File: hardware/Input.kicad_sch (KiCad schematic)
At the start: 41 parts, among them J24 Conn_01x02, J27 USB_C_Receptacle_USB2.0, J4 AudioJack3, J5 Conn_Coaxial, J6 Conn_Coaxial, J7 Conn_Coaxial, J8 Conn_Coaxial, J9 Barrel_Jack_Switch, U23 74LVCH2T45DC, U24 74LVCH2T45DC, U25 74LVCH2T45DC

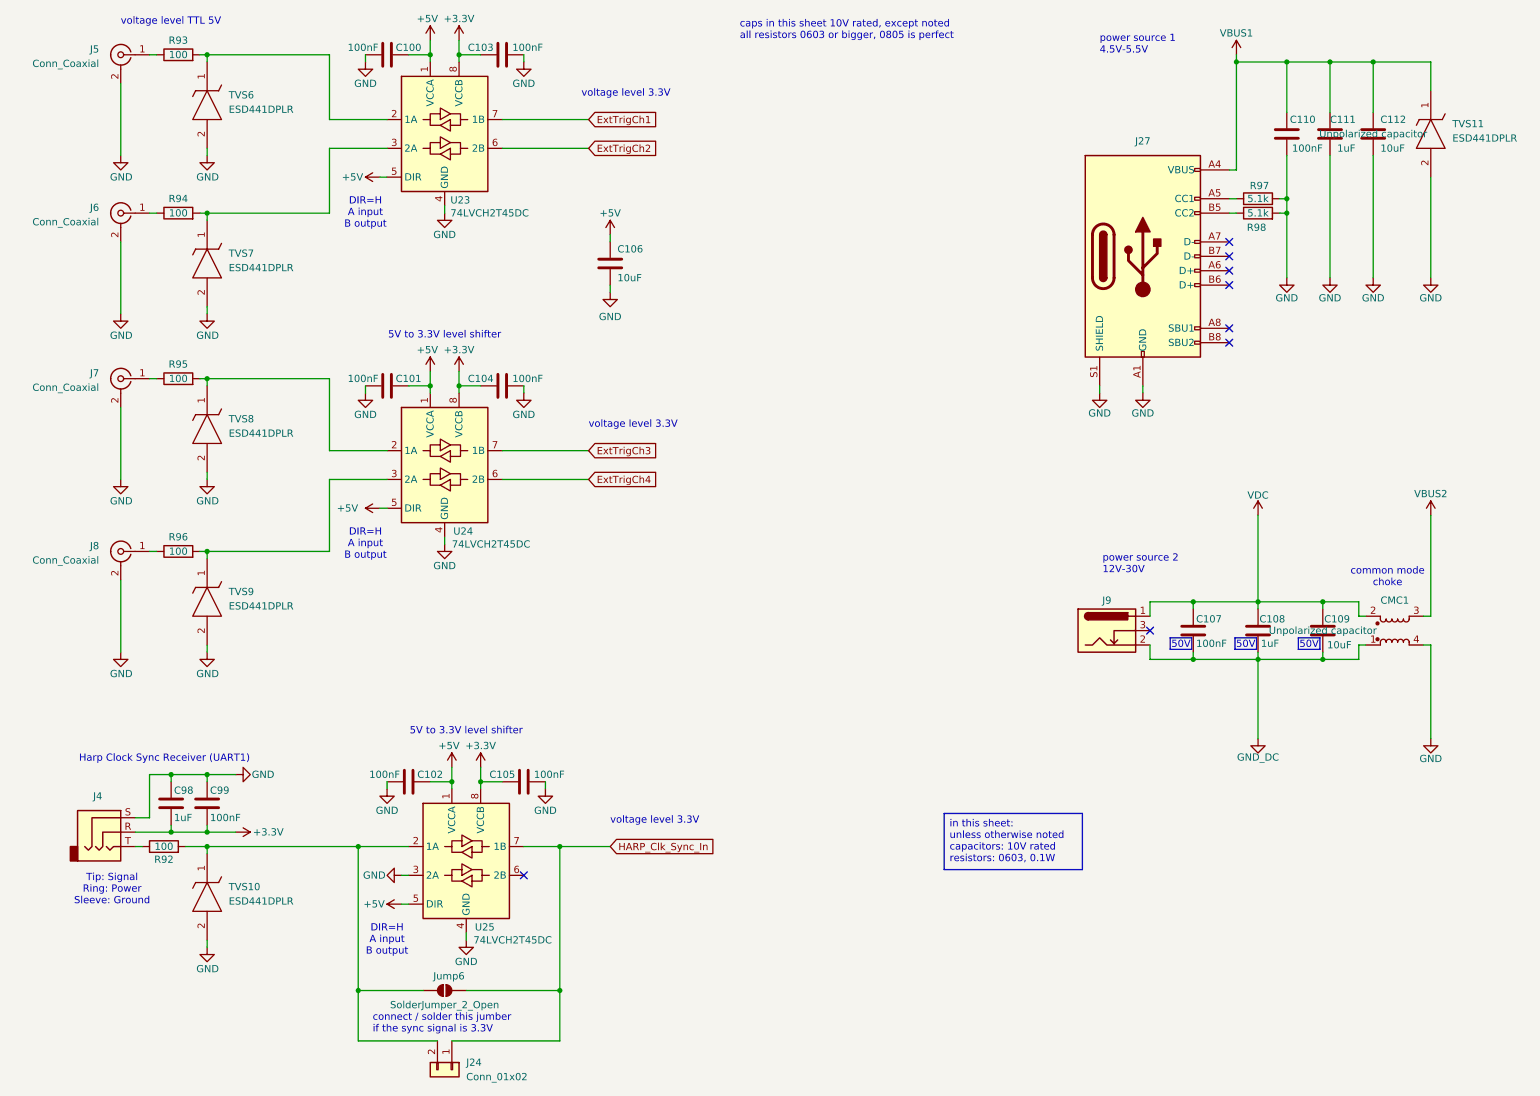
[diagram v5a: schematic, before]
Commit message: Jumpers and interstages connections + added zeners to supply sections + justified text
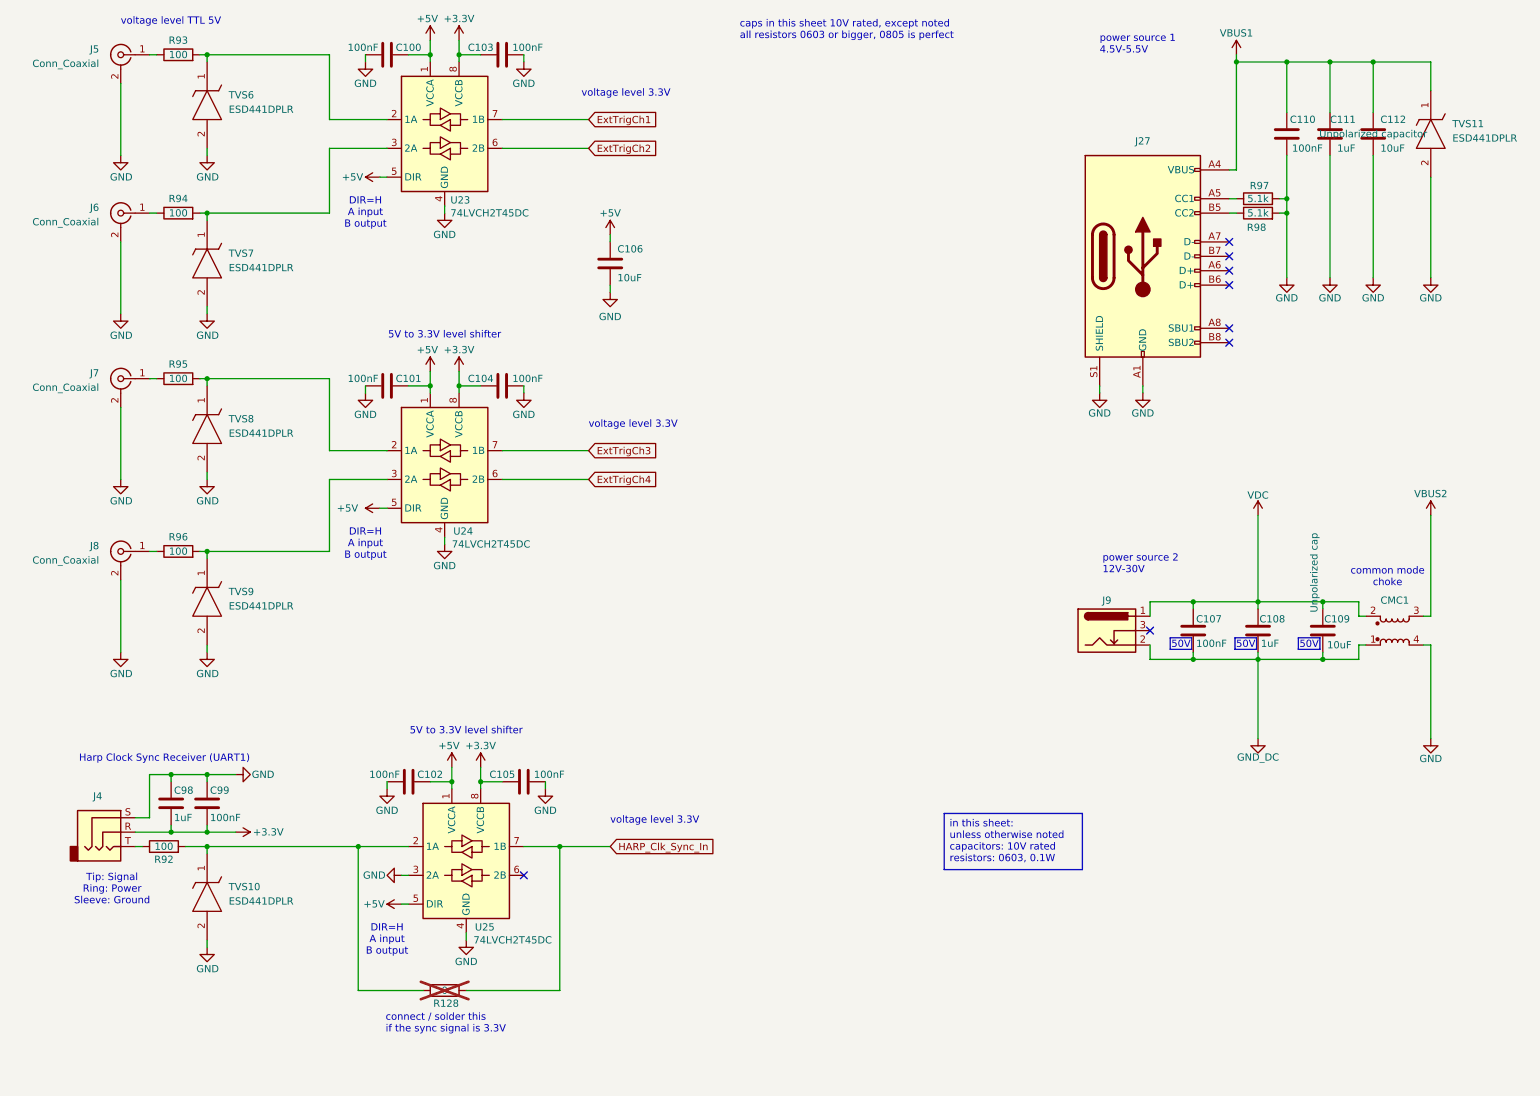
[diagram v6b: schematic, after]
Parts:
- removed J24: Conn_01x02, Connector_PinHeader_2.54mm:PinHeader_1x02_P2.54mm_Vertical, symbol harp.device.quad.dac:Conn_01x02
- removed Jump6: SolderJumper_2_Open, harp.device.quad.dac.kicad:R_0603_1608Metric_Pad0.98x0.95mm_HandSolder, symbol harp.device.quad.dac:SolderJumper_2_Open
- added R128: 0, Resistor_SMD:R_0603_1608Metric, symbol harp.device.quad.dac:R_0603
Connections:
- net HARP_Clk_Sync_In: now also R128.2
- net at R92.2, TVS10.1, U25.2 (1A): now also R128.1
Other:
- note added: "connect / solder this if the sync signal is 3.3V"
- note removed: "connect / solder this jumber if the sync signal is 3.3V"
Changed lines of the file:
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@@
 		)
 	)
-	(text "connect / solder this jumber\nif the sync signal is 3.3V"
+	(text "connect / solder this\nif the sync signal is 3.3V"
 		(exclude_from_sim no)
-		(at 76.2 194.31 0)
+		(at 78.486 194.31 0)
 		(effects
 			(font
@@
 	)
 	(junction
-		(at 73.66 186.69)
-		(diameter 0)
-		(color 0 0 0 0)
-	)
-	(junction
 		(at 220.98 118.11)
 		(diameter 0)
@@
 	)
 	(junction
-		(at 109.22 186.69)
-		(diameter 0)
-		(color 0 0 0 0)
-	)
-	(junction
 		(at 252.73 22.86)
 		(diameter 0)
@@
 	(wire
 		(pts
-			(xy 109.22 195.58) (xy 109.22 186.69)
-		)
-		(stroke
-			(width 0)
-			(type default)
-		)
-	)
-	(wire
-		(pts
 			(xy 109.22 186.69) (xy 92.71 186.69)
 		)
@@
 	(wire
 		(pts
-			(xy 90.17 195.58) (xy 109.22 195.58)
-		)
-		(stroke
-			(width 0)
-			(type default)
-		)
-	)
-	(wire
-		(pts
 			(xy 102.87 161.29) (xy 109.22 161.29)
 		)
@@
 	(wire
 		(pts
-			(xy 87.63 195.58) (xy 73.66 195.58)
-		)
-		(stroke
-			(width 0)
-			(type default)
-		)
-	)
-	(wire
-		(pts
 			(xy 95.25 149.86) (xy 95.25 151.13)
 		)
@@
 	(wire
 		(pts
-			(xy 73.66 195.58) (xy 73.66 186.69)
-		)
-		(stroke
-			(width 0)
-			(type default)
-		)
-	)
-	(wire
-		(pts
 			(xy 68.58 38.1) (xy 68.58 49.53)
 		)
@@
 	)
 	(symbol
-		(lib_id "harp.device.quad.dac:Conn_01x02")
-		(at 90.17 200.66 270)
-		(unit 1)
-		(exclude_from_sim no)
-		(in_bom yes)
-		(on_board yes)
-		(dnp no)
-		(fields_autoplaced yes)
-		(property "Reference" "J24"
-			(at 92.71 199.3899 90)
-			(effects
-				(font
-					(size 1.27 1.27)
-				)
-				(justify left)
-			)
-		)
-		(property "Value" "Conn_01x02"
-			(at 92.71 201.9299 90)
-			(effects
-				(font
-					(size 1.27 1.27)
-				)
-				(justify left)
-			)
-		)
-		(property "Footprint" "Connector_PinHeader_2.54mm:PinHeader_1x02_P2.54mm_Vertical"
-			(at 90.17 200.66 0)
-			(effects
-				(font
-					(size 1.27 1.27)
-				)
-				(hide yes)
-			)
-		)
-		(property "Datasheet" "~"
-			(at 90.17 200.66 0)
-			(effects
-				(font
-					(size 1.27 1.27)
-				)
-				(hide yes)
-			)
-		)
-		(property "Description" "Generic connector, single row, 01x02, script generated (kicad-library-utils/schlib/autogen/connector/)"
-			(at 90.17 200.66 0)
-			(effects
-				(font
-					(size 1.27 1.27)
-				)
-				(hide yes)
-			)
-		)
-		(pin "2"
-		)
-		(pin "1"
-		)
-		(instances
-			(project ""
-				(path "/6b47c519-21c4-43bd-9777-b273999e4447/8b495cef-3a6a-4801-9796-978978016448"
-					(reference "J24")
-					(unit 1)
-				)
-			)
-		)
-	)
-	(symbol
 		(lib_id "power:GND")
 		(at 92.71 177.8 0)
@@
 			)
 		)
-		(property "Description" "Unpolarized capacitor"
-			(at 243.84 123.19 0)
+		(property "Description" "Unpolarized cap"
+			(at 242.316 105.918 90)
 			(effects
 				(font
 					(size 1.27 1.27)
 				)
+				(justify right)
 			)
 		)
@@
 	)
 	(symbol
+		(lib_id "harp.device.quad.dac:R_0603")
+		(at 88.9 186.69 90)
+		(unit 1)
+		(exclude_from_sim yes)
+		(in_bom no)
+		(on_board no)
+		(dnp yes)
+		(property "Reference" "R128"
+			(at 89.154 188.976 90)
+			(effects
+				(font
+					(size 1.27 1.27)
+				)
+			)
+		)
+		(property "Value" "0"
+			(at 88.9 186.69 90)
+			(effects
+				(font
+					(size 1.27 1.27)
+				)
+			)
+		)
+		(property "Footprint" "Resistor_SMD:R_0603_1608Metric"
+			(at 88.9 188.468 90)
+			(effects
+				(font
+					(size 1.27 1.27)
+				)
+				(hide yes)
+			)
+		)
+		(property "Datasheet" "~"
+			(at 88.9 186.69 0)
+			(effects
+				(font
+					(size 1.27 1.27)
+				)
+				(hide yes)
+			)
+		)
+		(property "Description" "Resistor"
+			(at 88.9 186.69 0)
+			(effects
+				(font
+					(size 1.27 1.27)
+				)
+				(hide yes)
+			)
+		)
+		(property "Tolerance" "1%"
+			(at 88.9 186.69 90)
+			(effects
+				(font
+					(size 1.27 1.27)
+				)
+				(hide yes)
+			)
+		)
+		(property "Link" "https://www.digikey.com/en/products/detail/yageo/RT0402BRD071KL/1069118"
+			(at 88.9 186.69 90)
+			(effects
+				(font
+					(size 1.27 1.27)
+				)
+				(hide yes)
+			)
+		)
+		(property "Manufacturer" "Yageo"
+			(at 88.9 186.69 0)
+			(effects
+				(font
+					(size 1.27 1.27)
+				)
+				(hide yes)
+			)
+		)
+		(property "Manufacturer Number" "RT0402BRD071KL"
+			(at 88.9 186.69 0)
+			(effects
+				(font
+					(size 1.27 1.27)
+				)
+				(hide yes)
+			)
+		)
+		(property "PCBWay Link" ""
+			(at 88.9 186.69 0)
+			(effects
+				(font
+					(size 1.27 1.27)
+				)
+				(hide yes)
+			)
+		)
+		(pin "1"
+		)
+		(pin "2"
+		)
+		(instances
+			(project "harp.device.quad.dac"
+				(path "/6b47c519-21c4-43bd-9777-b273999e4447/8b495cef-3a6a-4801-9796-978978016448"
+					(reference "R128")
+					(unit 1)
+				)
+			)
+		)
+	)
+	(symbol
 		(lib_id "power:GND")
 		(at 31.75 127 0)
@@
 					(unit 1)
 				)
-			)
-		)
-	)
-	(symbol
-		(lib_id "harp.device.quad.dac:SolderJumper_2_Open")
-		(at 88.9 186.69 0)
-		(unit 1)
-		(exclude_from_sim no)
-		(in_bom yes)
-		(on_board yes)
-		(dnp no)
-		(property "Reference" "Jump6"
-			(at 89.662 184.15 0)
-			(effects
-				(font
-					(size 1.27 1.27)
-				)
-			)
-		)
-		(property "Value" "SolderJumper_2_Open"
-			(at 88.9 189.23 0)
-			(effects
-				(font
-					(size 1.27 1.27)
-				)
-			)
-		)
-		(property "Footprint" "harp.device.quad.dac.kicad:R_0603_1608Metric_Pad0.98x0.95mm_HandSolder"
-			(at 88.9 186.69 0)
-			(effects
-				(font
-					(size 1.27 1.27)
-				)
-				(hide yes)
-			)
-		)
-		(property "Datasheet" "~"
-			(at 88.9 186.69 0)
-			(effects
-				(font
-					(size 1.27 1.27)
-				)
-				(hide yes)
-			)
-		)
-		(property "Description" "Solder Jumper, 2-pole, open"
-			(at 88.9 186.69 0)
-			(effects
-				(font
-					(size 1.27 1.27)
-				)
-				(hide yes)
-			)
-		)
-		(pin "2"
-		)
-		(pin "1"
-		)
-		(instances
-			(project "harp.device.quad.dac"
-				(path "/6b47c519-21c4-43bd-9777-b273999e4447/8b495cef-3a6a-4801-9796-978978016448"
-					(reference "Jump6")
-					(unit 1)
-				)
-			)
-			(project "multi_ch_harp_dac"
-				(path "/bcebacf6-3a3d-4b86-825a-a573788c489f/3d5c816b-acda-40a0-af6b-bbc77a846000"
-					(reference "Jump?")
-					(unit 1)
-				)

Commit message: The part designators have been reannotated.
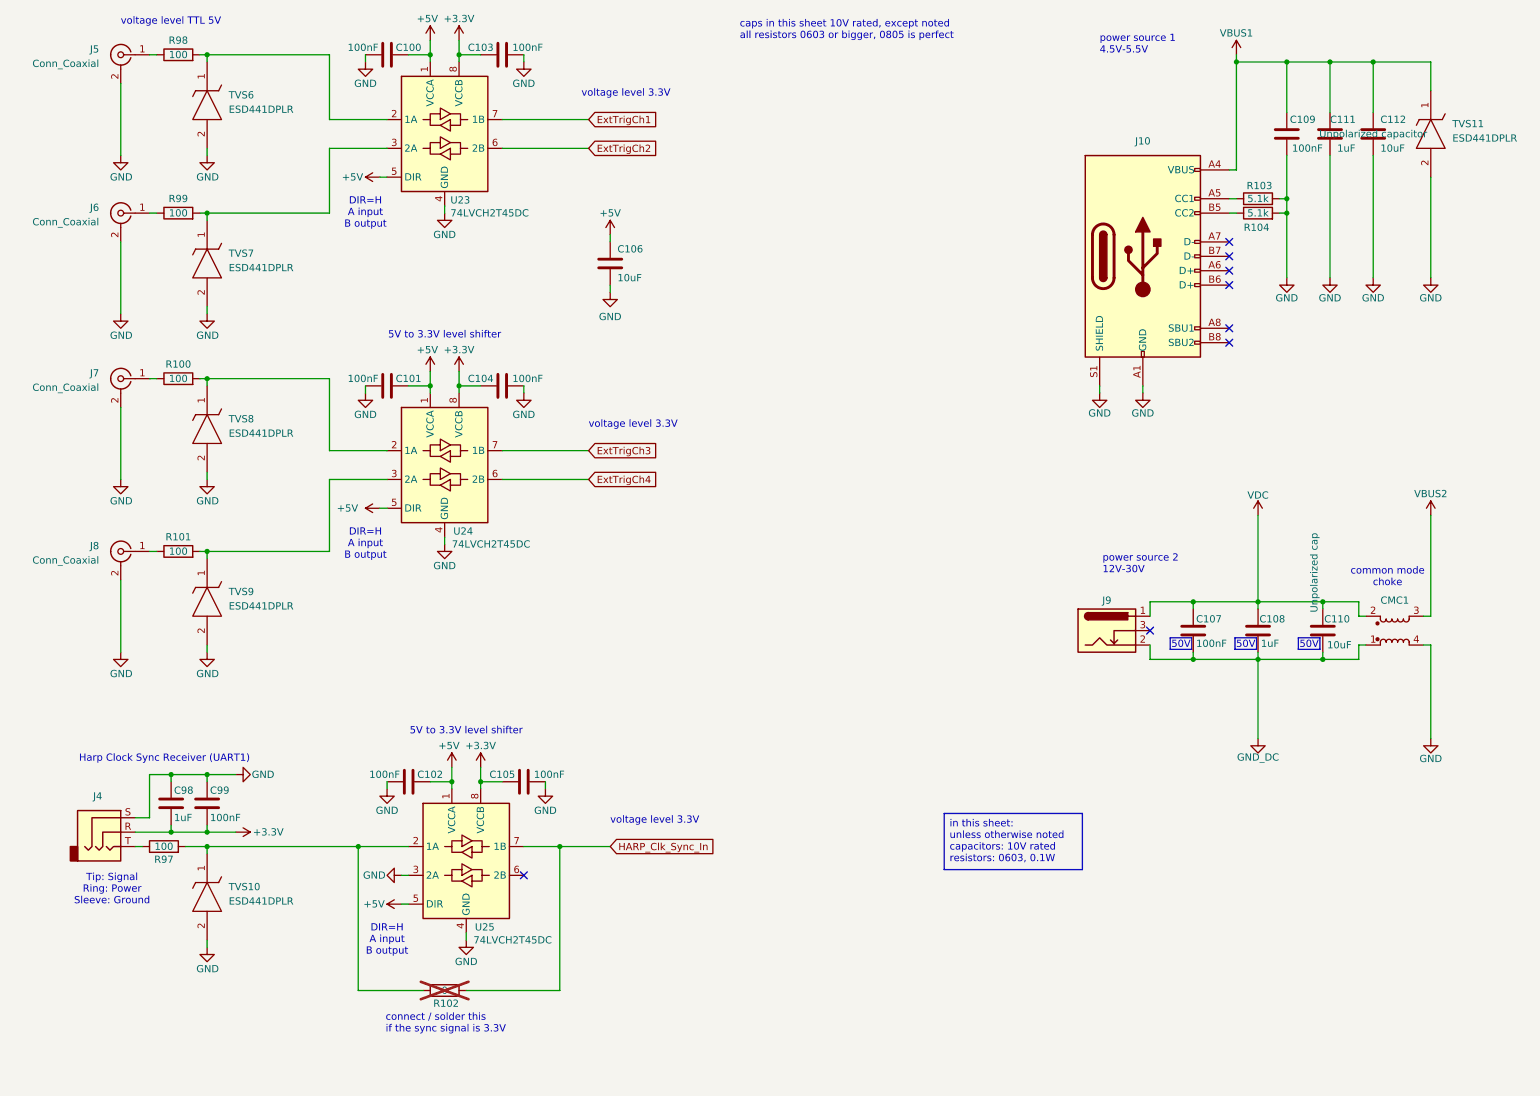
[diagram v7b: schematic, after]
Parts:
- renumbered C110 to C109, C109 to C110, J27 to J10, R95 to R100, R96 to R101, R128 to R102, R97 to R103, R98 to R104, R92 to R97, R93 to R98, R94 to R99
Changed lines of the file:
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@@
 		(dnp no)
 		(fields_autoplaced yes)
-		(property "Reference" "J27"
+		(property "Reference" "J10"
 			(at 212.09 36.83 0)
 			(effects
@@
 			(project "harp.device.quad.dac"
 				(path "/6b47c519-21c4-43bd-9777-b273999e4447/8b495cef-3a6a-4801-9796-978978016448"
-					(reference "J27")
+					(reference "J10")
 					(unit 1)
 				)
@@
 		(on_board yes)
 		(dnp no)
-		(property "Reference" "C110"
+		(property "Reference" "C109"
 			(at 242.57 33.02 0)
 			(effects
@@
 			(project "harp.device.quad.dac"
 				(path "/6b47c519-21c4-43bd-9777-b273999e4447/8b495cef-3a6a-4801-9796-978978016448"
-					(reference "C110")
+					(reference "C109")
 					(unit 1)
 				)
@@
 		(on_board yes)
 		(dnp no)
-		(property "Reference" "R98"
+		(property "Reference" "R104"
 			(at 232.156 52.07 90)
 			(effects
@@
 			(project "harp.device.quad.dac"
 				(path "/6b47c519-21c4-43bd-9777-b273999e4447/8b495cef-3a6a-4801-9796-978978016448"
-					(reference "R98")
+					(reference "R104")
 					(unit 1)
 				)
@@
 		(on_board yes)
 		(dnp no)
-		(property "Reference" "C109"
+		(property "Reference" "C110"
 			(at 244.094 121.158 0)
 			(effects
@@
 			(project "harp.device.quad.dac"
 				(path "/6b47c519-21c4-43bd-9777-b273999e4447/8b495cef-3a6a-4801-9796-978978016448"
-					(reference "C109")
+					(reference "C110")
 					(unit 1)
 				)
@@
 		(on_board yes)
 		(dnp no)
-		(property "Reference" "R96"
+		(property "Reference" "R101"
 			(at 41.91 106.68 90)
 			(effects
@@
 			(project "harp.device.quad.dac"
 				(path "/6b47c519-21c4-43bd-9777-b273999e4447/8b495cef-3a6a-4801-9796-978978016448"
-					(reference "R96")
+					(reference "R101")
 					(unit 1)
 				)
@@
 		(on_board yes)
 		(dnp no)
-		(property "Reference" "R94"
+		(property "Reference" "R99"
 			(at 41.91 46.99 90)
 			(effects
@@
 			(project "harp.device.quad.dac"
 				(path "/6b47c519-21c4-43bd-9777-b273999e4447/8b495cef-3a6a-4801-9796-978978016448"
-					(reference "R94")
+					(reference "R99")
 					(unit 1)
 				)
@@
 		(on_board no)
 		(dnp yes)
-		(property "Reference" "R128"
+		(property "Reference" "R102"
 			(at 89.154 188.976 90)
 			(effects
@@
 			(project "harp.device.quad.dac"
 				(path "/6b47c519-21c4-43bd-9777-b273999e4447/8b495cef-3a6a-4801-9796-978978016448"
-					(reference "R128")
+					(reference "R102")
 					(unit 1)
 				)
@@
 		(on_board yes)
 		(dnp no)
-		(property "Reference" "R92"
+		(property "Reference" "R97"
 			(at 39.37 163.576 90)
 			(effects
@@
 			(project "harp.device.quad.dac"
 				(path "/6b47c519-21c4-43bd-9777-b273999e4447/8b495cef-3a6a-4801-9796-978978016448"
-					(reference "R92")
+					(reference "R97")
 					(unit 1)
 				)
@@
 		(on_board yes)
 		(dnp no)
-		(property "Reference" "R93"
+		(property "Reference" "R98"
 			(at 41.91 19.05 90)
 			(effects
@@
 			(project "harp.device.quad.dac"
 				(path "/6b47c519-21c4-43bd-9777-b273999e4447/8b495cef-3a6a-4801-9796-978978016448"
-					(reference "R93")
+					(reference "R98")
 					(unit 1)
 				)
@@
 		(on_board yes)
 		(dnp no)
-		(property "Reference" "R97"
+		(property "Reference" "R103"
 			(at 232.664 44.704 90)
 			(effects
@@
 			(project "harp.device.quad.dac"
 				(path "/6b47c519-21c4-43bd-9777-b273999e4447/8b495cef-3a6a-4801-9796-978978016448"
-					(reference "R97")
+					(reference "R103")
 					(unit 1)
 				)
@@
 		(on_board yes)
 		(dnp no)
-		(property "Reference" "R95"
+		(property "Reference" "R100"
 			(at 41.91 76.2 90)
 			(effects
@@
 			(project "harp.device.quad.dac"
 				(path "/6b47c519-21c4-43bd-9777-b273999e4447/8b495cef-3a6a-4801-9796-978978016448"
-					(reference "R95")
+					(reference "R100")
 					(unit 1)
 				)
